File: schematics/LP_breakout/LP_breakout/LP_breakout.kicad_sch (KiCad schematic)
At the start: 5 parts, among them J1 RJ45, J2 Conn_01x03_Socket, J3 Conn_02x04_Counter_Clockwise, J4 Conn_02x15_Counter_Clockwise, J5 Conn_02x02_Counter_Clockwise

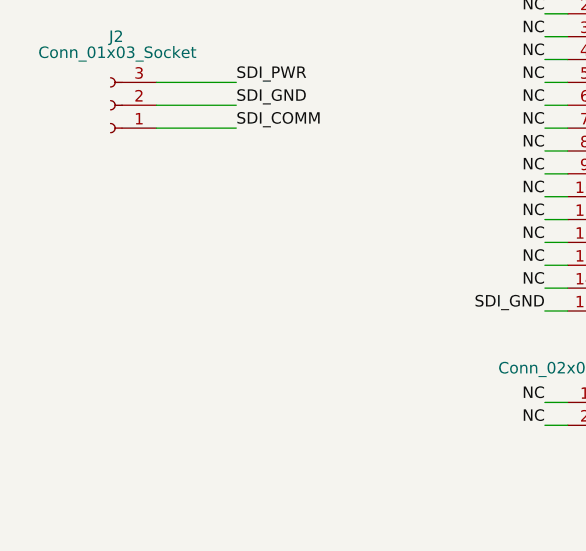
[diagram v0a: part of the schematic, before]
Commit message: Updated LP_breakout
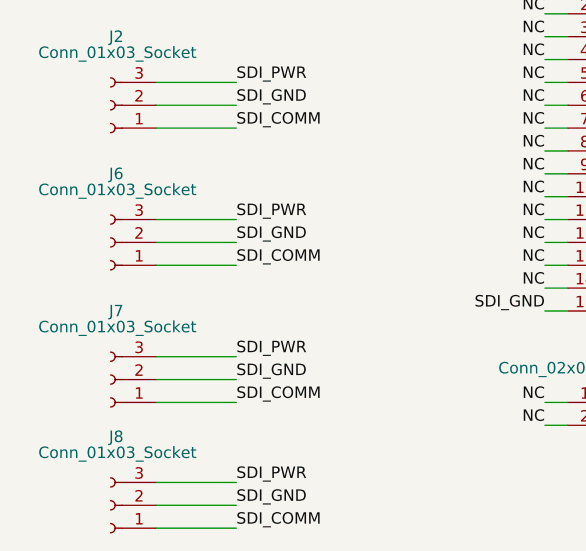
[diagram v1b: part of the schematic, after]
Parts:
- added J6, J7, J8: Conn_01x03_Socket, Library:MC1,5_3-G-3,5, symbol Connector:Conn_01x03_Socket
- J1: footprint (none) -> Connector_RJ:RJ45_Amphenol_RJHSE538X
- J2: footprint (none) -> Library:MC1,5_3-G-3,5
- J3: footprint (none) -> Connector_PinSocket_2.54mm:PinSocket_2x04_P2.54mm_Vertical
- J4: footprint (none) -> Connector_PinHeader_2.54mm:PinHeader_2x15_P2.54mm_Vertical
- J5: footprint (none) -> Connector_PinHeader_2.54mm:PinHeader_2x02_P2.54mm_Vertical
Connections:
- net SDI_COMM: now also J6.1 (Pin_1), J7.1 (Pin_1), J8.1 (Pin_1)
- net SDI_GND: now also J6.2 (Pin_2), J7.2 (Pin_2), J8.2 (Pin_2)
- net SDI_PWR: now also J6.3 (Pin_3), J7.3 (Pin_3), J8.3 (Pin_3)
